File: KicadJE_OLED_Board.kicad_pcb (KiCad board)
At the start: 2 copper layers, 170.6 x 128 mm, 296 parts, among them J1 LED 1-6, J101 Out1, J102 IN1, J103 OUT1, J104 OutFlt, J105 INFLT, J106 OUTFLT, J107 In1, J108 InFlt, J201 OLED, J202 ADC Input, J203 Out2, J204 Out1, J205 OUT1, J206 OUT2, J207 IN1, J208 IN2, J209 CV1, J210 CV2, J211 FrontLED, J212 -12V Front, J301 UART, J302 AVR-ISP-6, J401 Out2, J402 Out1, J403 OUT1, J404 OUT2, J405 IN1, J406 IN2, J407 CV1, J408 CV2, J409 -12V Front, J410 OLED, J411 ADC Input, J412 FrontLED, J501 UART, J502 AVR-ISP-6, P1 Doepfer_Power_16pin, P101 Doepfer_Power_10pin, P201 Doepfer_Power_16pin, P401 Doepfer_Power_16pin, SW201 Rotary_Encoder_Switch, SW202 Rotary_Encoder_Switch, SW401 Rotary_Encoder_Switch, SW402 Rotary_Encoder_Switch, U101 TL072, U201 TL072, U202 TL072, U301 ATmega32A-AU, U401 TL072, U402 MCP4822, U501 ATmega32A-AU, Y301 16MHz, Y501 16MHz

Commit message: Power Amp/FLT
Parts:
- turned D103 to 0 degrees
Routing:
- net -12VA: track 109.3 -> 153.2 mm, vias 1 -> 4
- net +12VA: track 25.3 -> 47.8 mm, vias 0 -> 2
- net /InPos: track 0.00 -> 18.1 mm
- net /InNeg: track 0.00 -> 14.2 mm
- net Net-(D103-Pad2): track 0.00 -> 2.88 mm, vias 0 -> 1
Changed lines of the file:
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@@
     (thickness 1.6)
     (drawings 109)
-    (tracks 99)
+    (tracks 136)
     (zones 0)
     (modules 296)
@@
   )
   (module AJ:D_0805_AJ (layer F.Cu)
-    (at 151 51 180)
+    (at 151 51)
     (descr "Diode SMD 0805 (2012 Metric), square (rectangular) end terminal, IPC_7351 nominal, (Body size source: https://docs.google.com/spreadsheets/d/1BsfQQcO9C6DZCsRaXUlFlo91Tg2WpOkGARC1WS5S8t0/edit?usp=sharing), generated with kicad-footprint-generator")
     (tags "diode handsolder")
@@
       (effects (font (size 0.5 0.5) (thickness 0.08)))
     )
-    (pad 1 smd roundrect (at -1.025 0 180) (size 1.15 1.4) (layers F.Cu F.Paste F.Mask) (roundrect_rratio 0.217391)
+    (pad 1 smd roundrect (at -1.025 0) (size 1.15 1.4) (layers F.Cu F.Paste F.Mask) (roundrect_rratio 0.217391)
       (net 3 -12VA))
-    (pad 2 smd roundrect (at 1.025 0 180) (size 1.15 1.4) (layers F.Cu F.Paste F.Mask) (roundrect_rratio 0.217391)
+    (pad 2 smd roundrect (at 1.025 0) (size 1.15 1.4) (layers F.Cu F.Paste F.Mask) (roundrect_rratio 0.217391)
       (net 37 "Net-(D103-Pad2)"))
     (model ${KISYS3DMOD}/Diode_SMD.3dshapes/D_0805_2012Metric.wrl
@@
   (segment (start 249.125 130.8) (end 249.875001 130.049999) (width 0.15) (layer B.Cu) (net 2))
   (segment (start 248.075 121.07) (end 253.125 121.07) (width 0.15) (layer B.Cu) (net 2))
+  (segment (start 156 70) (end 156 76.5) (width 0.4) (layer B.Cu) (net 2))
+  (via (at 156 76.5) (size 0.8) (drill 0.4) (layers F.Cu B.Cu) (net 2))
+  (segment (start 156 89) (end 156 76.5) (width 0.4) (layer F.Cu) (net 2))
+  (segment (start 155 90) (end 156 89) (width 0.4) (layer F.Cu) (net 2))
+  (via (at 156 89) (size 0.8) (drill 0.4) (layers F.Cu B.Cu) (net 2))
+  (segment (start 154.905 87.905) (end 156 89) (width 0.4) (layer B.Cu) (net 2))
+  (segment (start 154.3 87.905) (end 154.905 87.905) (width 0.4) (layer B.Cu) (net 2))
   (segment (start 248.075 110.91) (end 253.125 110.91) (width 0.15) (layer B.Cu) (net 3))
   (segment (start 252.075 109.86) (end 253.125 110.91) (width 0.15) (layer B.Cu) (net 3))
@@
   (segment (start 259.6 55.8) (end 265.1 55.8) (width 0.15) (layer B.Cu) (net 3))
   (segment (start 250.6 46.8) (end 259.6 55.8) (width 0.15) (layer B.Cu) (net 3))
+  (segment (start 149.975 51) (end 143 51) (width 0.4) (layer F.Cu) (net 3))
+  (via (at 142 52) (size 0.8) (drill 0.4) (layers F.Cu B.Cu) (net 3))
+  (segment (start 143 51) (end 142 52) (width 0.4) (layer F.Cu) (net 3))
+  (segment (start 142 68) (end 144 70) (width 0.4) (layer B.Cu) (net 3))
+  (segment (start 142 52) (end 142 68) (width 0.4) (layer B.Cu) (net 3))
+  (via (at 148 82.5) (size 0.8) (drill 0.4) (layers F.Cu B.Cu) (net 3))
+  (segment (start 147.119999 81.619999) (end 148 82.5) (width 0.4) (layer F.Cu) (net 3))
+  (segment (start 147.119999 81.524999) (end 147.119999 81.619999) (width 0.4) (layer F.Cu) (net 3))
+  (segment (start 148 83.795) (end 147.7 84.095) (width 0.4) (layer B.Cu) (net 3))
+  (segment (start 148 82.5) (end 148 83.795) (width 0.4) (layer B.Cu) (net 3))
+  (via (at 145.640686 70.3) (size 0.8) (drill 0.4) (layers F.Cu B.Cu) (net 3))
+  (segment (start 147.119999 71.779313) (end 145.640686 70.3) (width 0.4) (layer F.Cu) (net 3))
+  (segment (start 147.119999 81.524999) (end 147.119999 71.779313) (width 0.4) (layer F.Cu) (net 3))
+  (segment (start 144.3 70.3) (end 144 70) (width 0.4) (layer B.Cu) (net 3))
+  (segment (start 145.640686 70.3) (end 144.3 70.3) (width 0.4) (layer B.Cu) (net 3))
   (segment (start 232.6 114.8) (end 233.6 115.8) (width 0.15) (layer B.Cu) (net 4))
   (segment (start 232.6 111.3) (end 232.6 114.8) (width 0.15) (layer B.Cu) (net 4))
@@
   (segment (start 268.6 148.8) (end 268.6 146.8) (width 0.15) (layer B.Cu) (net 18))
   (via (at 267.6 145.8) (size 0.7) (drill 0.4) (layers F.Cu B.Cu) (net 18))
+  (via (at 151 52) (size 0.7) (drill 0.4) (layers F.Cu B.Cu) (net 37))
+  (segment (start 152 53) (end 151 52) (width 0.15) (layer B.Cu) (net 37))
+  (segment (start 152.025 53) (end 152 53) (width 0.15) (layer B.Cu) (net 37))
+  (segment (start 152 51) (end 151 52) (width 0.15) (layer F.Cu) (net 37))
+  (segment (start 152.025 51) (end 152 51) (width 0.15) (layer F.Cu) (net 37))
+  (segment (start 151.79 59.34) (end 149.25 59.34) (width 0.4) (layer F.Cu) (net 114))
+  (segment (start 149.24 59.35) (end 149.25 59.34) (width 0.4) (layer F.Cu) (net 114))
+  (segment (start 144 59.35) (end 149.24 59.35) (width 0.4) (layer F.Cu) (net 114))
+  (segment (start 156 63.55) (end 156 67.95) (width 0.4) (layer B.Cu) (net 114))
+  (segment (start 151.79 59.34) (end 156 63.55) (width 0.4) (layer B.Cu) (net 114))
+  (segment (start 149.25 69.5) (end 151.79 69.5) (width 0.4) (layer F.Cu) (net 115))
+  (segment (start 145.15 69.5) (end 144 70.65) (width 0.4) (layer F.Cu) (net 115))
+  (segment (start 149.25 69.5) (end 145.15 69.5) (width 0.4) (layer F.Cu) (net 115))
+  (segment (start 145.55 69.5) (end 144 67.95) (width 0.4) (layer B.Cu) (net 115))
+  (segment (start 149.25 69.5) (end 145.55 69.5) (width 0.4) (layer B.Cu) (net 115))
   (via (at 250.6 44.8) (size 0.7) (drill 0.4) (layers F.Cu B.Cu) (net 126))
   (segment (start 250.62499 44.82499) (end 250.6 44.8) (width 0.15) (layer B.Cu) (net 126))
@@
       )
     )
+  )
+  (zone (net 1) (net_name GND) (layer F.Cu) (hatch edge 0.508)
+    (connect_pads (clearance 0.508))
+    (min_thickness 0.254)
+    (fill yes (arc_segments 32) (thermal_gap 0.508) (thermal_bridge_width 0.508))
+    (polygon
+      (pts
+        (xy 158 73) (xy 142 73) (xy 142 51) (xy 158 51)
+      )
+    )
+  )
+  (zone (net 1) (net_name GND) (layer B.Cu) (hatch edge 0.508)
+    (connect_pads (clearance 0.508))
+    (min_thickness 0.254)
+    (fill yes (arc_segments 32) (thermal_gap 0.508) (thermal_bridge_width 0.508))
+    (polygon
+      (pts
+        (xy 158 73) (xy 142 73) (xy 142 51) (xy 158 51)
+      )
+    )

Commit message: Board
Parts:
- J107: value In1 -> In1_Flt
- J108: value InFlt -> InAmp
- moved D103 1.00 mm to (150.0, 51.0)
- moved R101 1.00 mm to (150.0, 53.0)
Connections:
- C104 pad 2: GND -> GNDA
- J108 pad 1: GND -> GNDA
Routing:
- net +12VA: track 47.8 -> 98.7 mm, vias 2 -> 3
- net Out1_Amp: track 0.00 -> 49.5 mm
- net Net-(D106-Pad2): track 0.00 -> 38.9 mm
- net -12VA: track 153.2 -> 191.8 mm
- net Out1_Filt: track 0.00 -> 33.5 mm
- net Net-(D104-Pad2): track 0.00 -> 26.3 mm
- net Net-(R117-Pad2): track 0.00 -> 21.0 mm
- net Net-(C104-Pad1): track 0.00 -> 20.0 mm
- net Net-(C101-Pad2): track 0.00 -> 18.0 mm
- net Net-(C101-Pad1): track 0.00 -> 14.5 mm
- net Net-(C102-Pad1): track 0.00 -> 8.24 mm
- net Net-(R107-Pad1): track 0.00 -> 7.40 mm
- net Net-(R116-Pad2): track 0.00 -> 6.62 mm
- net GNDA: track 0.00 -> 3.22 mm, vias 0 -> 2
- net Net-(J105-PadTN): track 0.00 -> 3.22 mm
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- added copper zone on B.Cu, net GNDA
- added copper zone on F.Cu, net GNDA

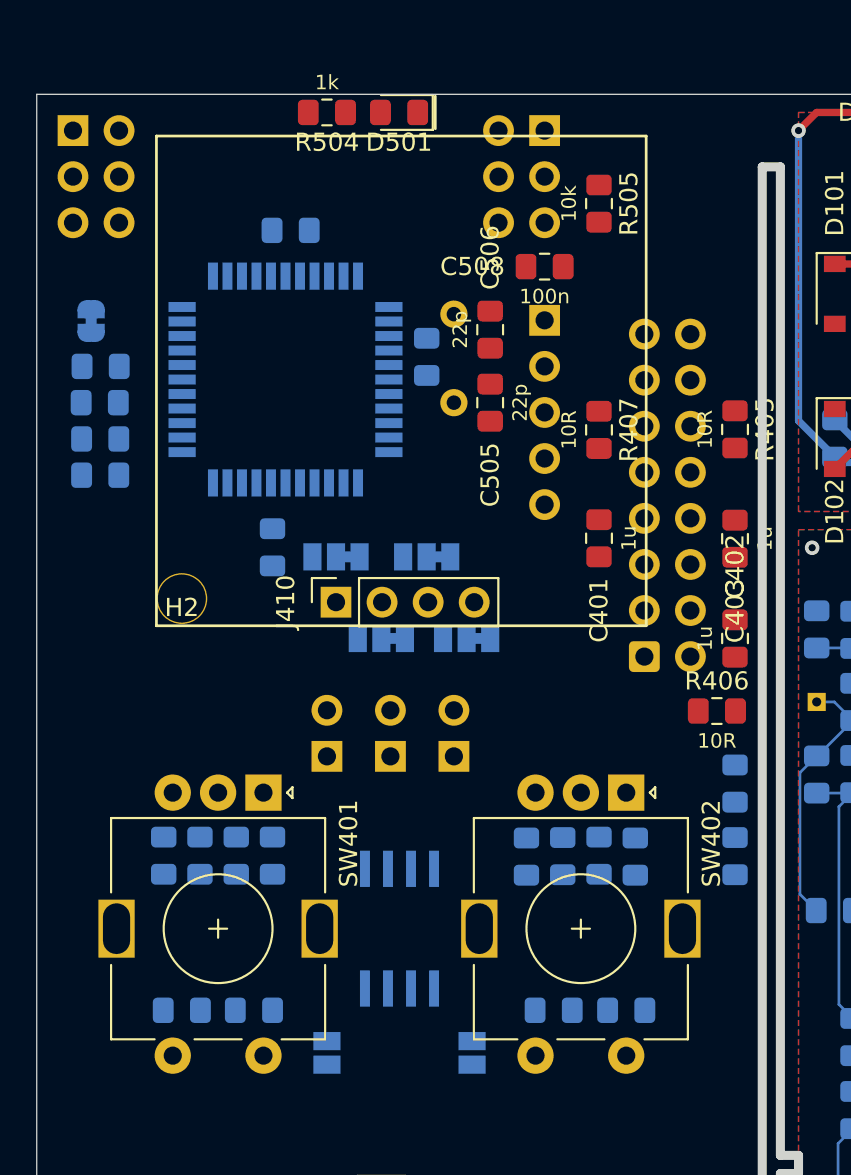
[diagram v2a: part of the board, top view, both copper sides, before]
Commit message: Wiring DAC board - initiated
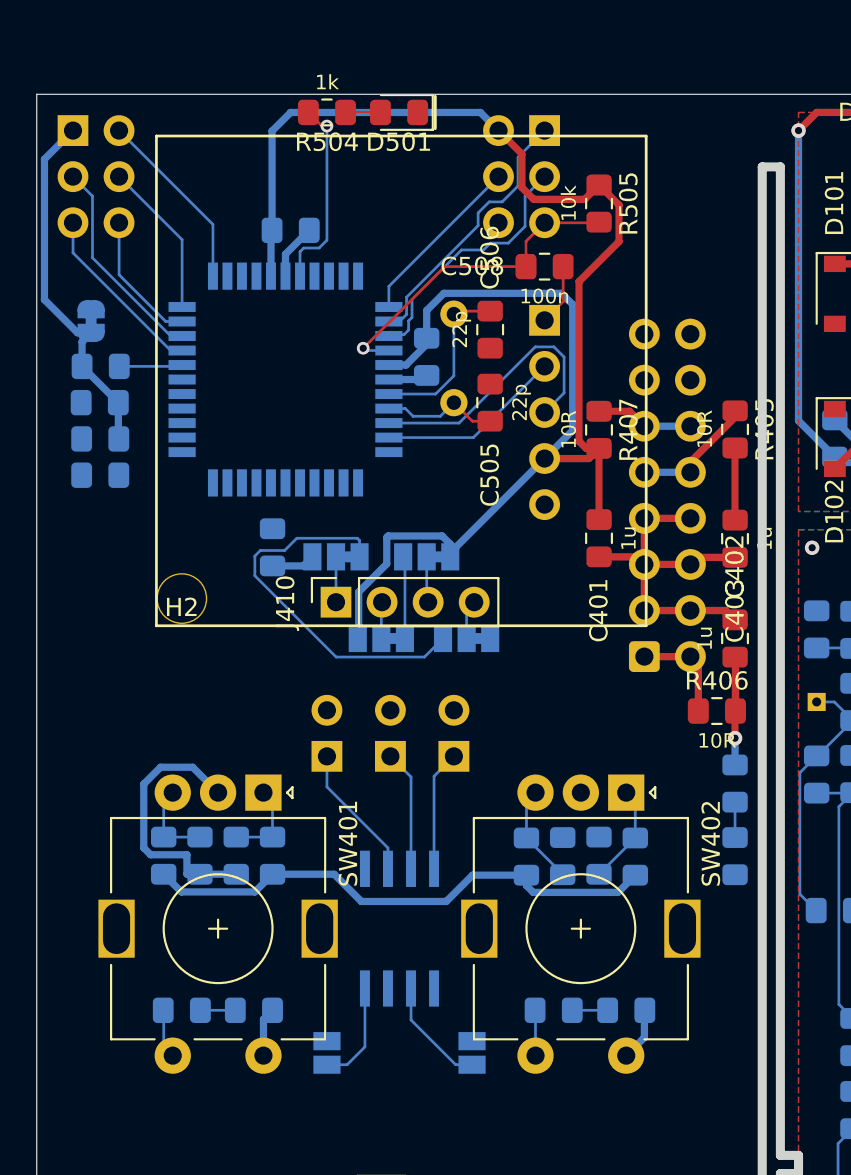
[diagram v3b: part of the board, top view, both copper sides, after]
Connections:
- net Net-(P201-Pad1) renamed /KicadJE_OLED_Mega32/InNeg
- net Net-(P201-Pad10) renamed /KicadJE_OLED_Mega32/InPos
- net Net-(P201-Pad11) renamed /KicadJE_OLED_Mega32/In5V
- net Net-(P401-Pad1) renamed /KicadJE_ATMega32A_DAC/InNeg
- net Net-(P401-Pad10) renamed /KicadJE_ATMega32A_DAC/InPos
- net Net-(P401-Pad11) renamed /KicadJE_ATMega32A_DAC/In5V
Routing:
- net +5V: track 0.00 -> 123.4 mm
- net GND: track 23.0 -> 71.9 mm
- net /KicadJE_ATMega32A_DAC/sheet6241082B/D17_SDA: track 0.00 -> 21.3 mm
- net GNDA: track 3.22 -> 23.4 mm
- net reset: track 0.00 -> 18.2 mm, vias 0 -> 1
- net /KicadJE_ATMega32A_DAC/sheet6241082B/D8_Rx: track 0.00 -> 15.1 mm
- net /KicadJE_ATMega32A_DAC/sheet6241082B/D6_MISO: track 0.00 -> 14.3 mm
- net /KicadJE_ATMega32A_DAC/sheet6241082B/D7_SCK: track 0.00 -> 14.1 mm
- net 30_A6_DAC: track 0.00 -> 11.6 mm
- net /KicadJE_ATMega32A_DAC/sheet6241082B/0_LED: track 0.00 -> 10.7 mm, vias 0 -> 1
- net /KicadJE_ATMega32A_DAC/sheet6241082B/D9_Tx: track 0.00 -> 10.2 mm
- net 27_A3_DAC: track 0.00 -> 10.2 mm
- net 31_A7_DAC: track 0.00 -> 9.91 mm
- net /KicadJE_ATMega32A_DAC/sheet6241082B/D5_MOSI: track 0.00 -> 9.69 mm
- net Net-(C506-Pad1): track 0.00 -> 9.47 mm
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
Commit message: Initial DAC layout
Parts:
- added C422: 100n, AJ:C_0805_AJ, B.Cu at (115.2, 92.0)
- moved R502 2.69 mm to (104.0, 65.0), turned to 0 degrees
- moved C507 2.27 mm to (103.2, 62.8)
- moved U402 0.25 mm to (120.2, 96.0)
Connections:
- J502 pad 3: /KicadJE_ATMega32A_DAC/sheet6241082B/D7_SCK -> SCK_DAC
- J502 pad 4: /KicadJE_ATMega32A_DAC/sheet6241082B/D5_MOSI -> MOSI_DAC
- JP407 pad 2: Net-(JP407-Pad2) -> CS_DAC
- JP408 pad 2: Net-(JP408-Pad2) -> MOSI_DAC
- JP409 pad 2: Net-(JP409-Pad2) -> SCK_DAC
- U501 pad 1: /KicadJE_ATMega32A_DAC/sheet6241082B/D5_MOSI -> MOSI_DAC
- U501 pad 3: /KicadJE_ATMega32A_DAC/sheet6241082B/D7_SCK -> SCK_DAC
- U501 pad 44: /KicadJE_ATMega32A_DAC/sheet6241082B/D4 -> CS_DAC
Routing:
- net /KicadJE_ATMega32A_DAC/sheet6241082B/D23: track 0.00 -> 118.6 mm
- net /KicadJE_ATMega32A_DAC/sheet6241082B/D22: track 0.00 -> 110.7 mm, vias 0 -> 2
- net /KicadJE_ATMega32A_DAC/sheet6241082B/D21: track 0.00 -> 108.2 mm, vias 0 -> 2
- net /KicadJE_ATMega32A_DAC/sheet6241082B/D19: track 0.00 -> 104.3 mm, vias 0 -> 2
- net /KicadJE_ATMega32A_DAC/sheet6241082B/D18: track 0.00 -> 104.1 mm, vias 0 -> 2
- net /KicadJE_ATMega32A_DAC/sheet6241082B/D20: track 0.00 -> 104.0 mm, vias 0 -> 2
- net 28_A4_DAC: track 8.62 -> 101.1 mm, vias 0 -> 6
- net +5V: track 123.4 -> 211.9 mm, vias 0 -> 2
- net 30_A6_DAC: track 11.6 -> 90.3 mm, vias 0 -> 6
- net 27_A3_DAC: track 10.2 -> 84.9 mm, vias 0 -> 4
- net GND: track 71.9 -> 146.6 mm, vias 0 -> 2
- net +12V: track 3.97 -> 77.7 mm, vias 0 -> 1
- net 29_A5_DAC: track 7.41 -> 75.6 mm, vias 0 -> 6
- net -12V: track 5.97 -> 60.1 mm, vias 1 -> 2
- net DACB: track 6.12 -> 51.8 mm
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
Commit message: Update KicadJE_OLED_Board.kicad_pcb
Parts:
- R302: moved to F.Cu
- moved C305 11.5 mm to (191.0, 63.7)
- moved J302 5.55 mm to (189.0, 53.8), turned to 180 degrees
- moved R302 4.95 mm to (167.0, 65.0), turned to 0 degrees
- moved C301 0.25 mm to (172.8, 56.0)
- moved C214 0.25 mm to (198.2, 79.5)
- moved C215 0.25 mm to (198.2, 74.5)
- moved R227 0.25 mm to (198.2, 69.5)
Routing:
- net GND: track 146.6 -> 258.3 mm, vias 2 -> 26
- net +5V: track 211.9 -> 274.7 mm, vias 2 -> 4
- net -12V: track 60.1 -> 108.3 mm
- net 24_A0_DAC: track 1.92 -> 49.8 mm, vias 0 -> 8
- net GNDA: track 65.7 -> 109.2 mm, vias 2 -> 33
- net Net-(C305-Pad2): track 0.00 -> 20.8 mm
- net /KicadJE_OLED_Mega32/ATMega32A.sch/D6_MISO: track 0.00 -> 16.8 mm
- net reset: track 18.2 -> 34.6 mm
- net /KicadJE_OLED_Mega32/ATMega32A.sch/D7_SCK: track 0.00 -> 13.7 mm
- net /KicadJE_OLED_Mega32/ATMega32A.sch/D5_MOSI: track 0.00 -> 12.6 mm
- net 30_A6: track 0.00 -> 10.9 mm
- net /KicadJE_OLED_Mega32/ATMega32A.sch/D9_Tx: track 0.00 -> 9.85 mm
- net /KicadJE_OLED_Mega32/ATMega32A.sch/D8_Rx: track 0.00 -> 9.84 mm
- net 27_A3: track 0.00 -> 9.35 mm
- net 31_A7: track 0.00 -> 9.09 mm
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
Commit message: Update KicadJE_OLED_Board.kicad_pcb
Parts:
- C220, C221, C222, C223, R303: moved to F.Cu
- moved R303 38.2 mm to (191.0, 58.5), turned to 270 degrees
- moved C217 11.0 mm to (172.0, 131.8), turned to 0 degrees
- moved C216 7.11 mm to (187.5, 131.5)
- moved R222 6.67 mm to (189.5, 131.5), turned to 270 degrees
- moved C224 4.51 mm to (175.5, 73.8), turned to 270 degrees
- moved C225 4.06 mm to (173.5, 73.8), turned to 270 degrees
- moved C221 3.09 mm to (186.8, 134.5), turned to 0 degrees
- moved R219 2.56 mm to (172.0, 129.8)
- moved C205 2.50 mm to (193.5, 131.5)
- moved R217 2.50 mm to (191.5, 131.5)
- moved C222 2.10 mm to (173.5, 138.0)
- moved C223 1.95 mm to (166.8, 134.0)
- moved C220 1.25 mm to (193.5, 138.8)
- moved C304 0.75 mm to (163.7, 66.0)
- moved C308 0.75 mm to (163.8, 64.0)
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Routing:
- net +12V: track 81.6 -> 187.8 mm, vias 1 -> 4
- net -12V: track 108.3 -> 202.1 mm, vias 2 -> 6
- net GND: track 258.3 -> 342.7 mm, vias 26 -> 30
- net +5V: track 274.7 -> 343.4 mm, vias 4 -> 8
- net /KicadJE_OLED_Mega32/ATMega32A.sch/D16_SCL: track 0.00 -> 30.9 mm
- net /KicadJE_OLED_Mega32/ATMega32A.sch/D17_SDA: track 0.00 -> 28.9 mm
- net GNDA: track 109.2 -> 128.2 mm
- net Net-(C217-Pad2): track 0.00 -> 15.5 mm
- net Net-(C216-Pad1): track 0.00 -> 14.9 mm
- net Net-(R216-Pad1): track 0.00 -> 14.7 mm
- net Net-(C206-Pad1): track 0.00 -> 13.4 mm
- net Net-(R218-Pad1): track 0.00 -> 10.7 mm
- net Net-(C217-Pad1): track 0.00 -> 10.3 mm
- net Net-(C216-Pad2): track 0.00 -> 10.1 mm
- net Net-(C205-Pad1): track 0.00 -> 10.0 mm
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
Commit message: Update KicadJE_OLED_Board.kicad_pcb
All boards routed initially
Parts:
- moved J203 0.30 mm to (183.0, 142.2)
- moved J204 0.26 mm to (177.0, 142.2)
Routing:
- net +5V: track 343.4 -> 469.7 mm, vias 8 -> 18
- net 28_A4: track 14.3 -> 136.1 mm, vias 0 -> 2
- net /KicadJE_OLED_Mega32/ATMega32A.sch/D23: track 0.00 -> 115.6 mm, vias 0 -> 2
- net /KicadJE_OLED_Mega32/ATMega32A.sch/D22: track 0.00 -> 114.5 mm, vias 0 -> 2
- net /KicadJE_OLED_Mega32/ATMega32A.sch/D21: track 0.00 -> 110.0 mm, vias 0 -> 2
- net /KicadJE_OLED_Mega32/ATMega32A.sch/D20: track 0.00 -> 107.0 mm, vias 0 -> 2
- net /KicadJE_OLED_Mega32/ATMega32A.sch/D19: track 0.00 -> 106.6 mm, vias 0 -> 2
- net /KicadJE_OLED_Mega32/ATMega32A.sch/D18: track 0.00 -> 105.5 mm, vias 0 -> 2
- net Net-(C225-Pad1): track 1.72 -> 99.9 mm, vias 0 -> 5
- net GND: track 342.7 -> 423.3 mm, vias 30 -> 70
- net Net-(C224-Pad1): track 1.75 -> 77.1 mm, vias 0 -> 4
- net 27_A3: track 15.9 -> 90.8 mm, vias 0 -> 2
- net 30_A6: track 17.7 -> 82.4 mm, vias 0 -> 4
- net GNDA: track 128.2 -> 191.0 mm, vias 33 -> 117
- net 29_A5: track 13.4 -> 71.4 mm, vias 0 -> 2
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
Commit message: DRC
DRC
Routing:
- net OUT1_DAC: track 7.01 -> 9.93 mm
- net GNDA: track 191.0 -> 191.7 mm
- net GND: vias 70 -> 69
